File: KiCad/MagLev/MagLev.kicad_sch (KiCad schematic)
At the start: 30 parts, among them J1 Barrel_Jack, Q5 ZX5T1951GTA, U10 DRV5505, U11 DRV5505, U12 DRV5505, U3 L78L05_SO8, U4 TL431A, U5 LM393, X1 L_Ferrite, X2 L_Ferrite, Y1 L_Ferrite, Y2 L_Ferrite

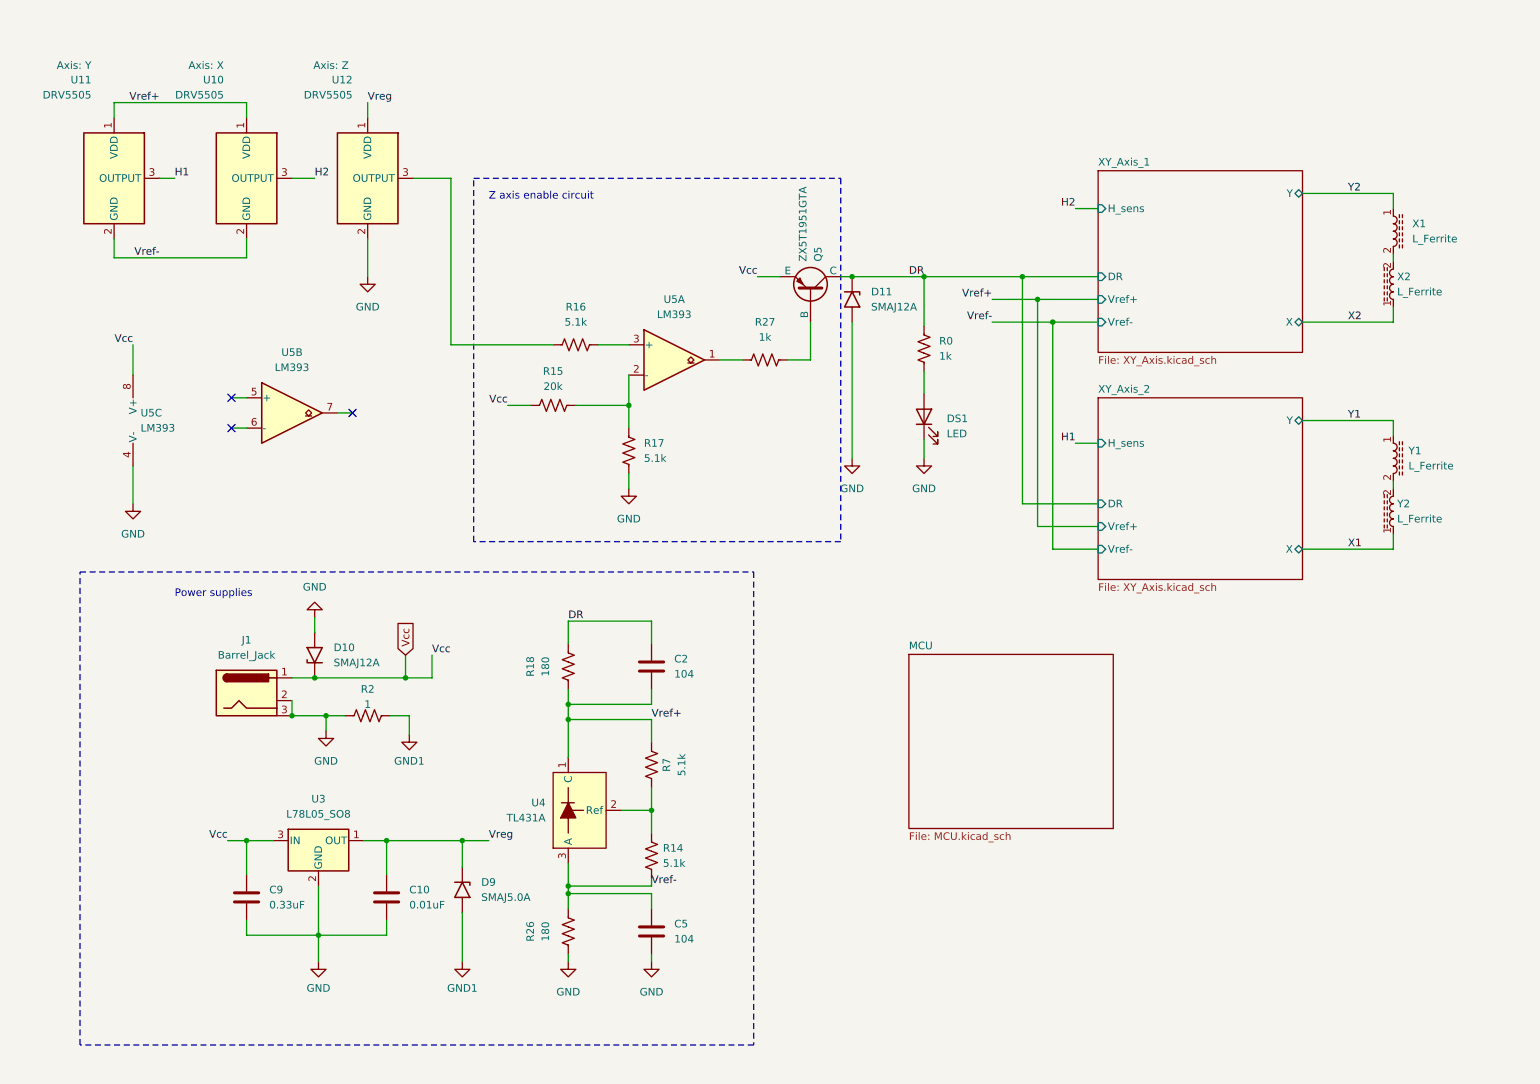
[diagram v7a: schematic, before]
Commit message: Add power fets and additional coils to schematic.
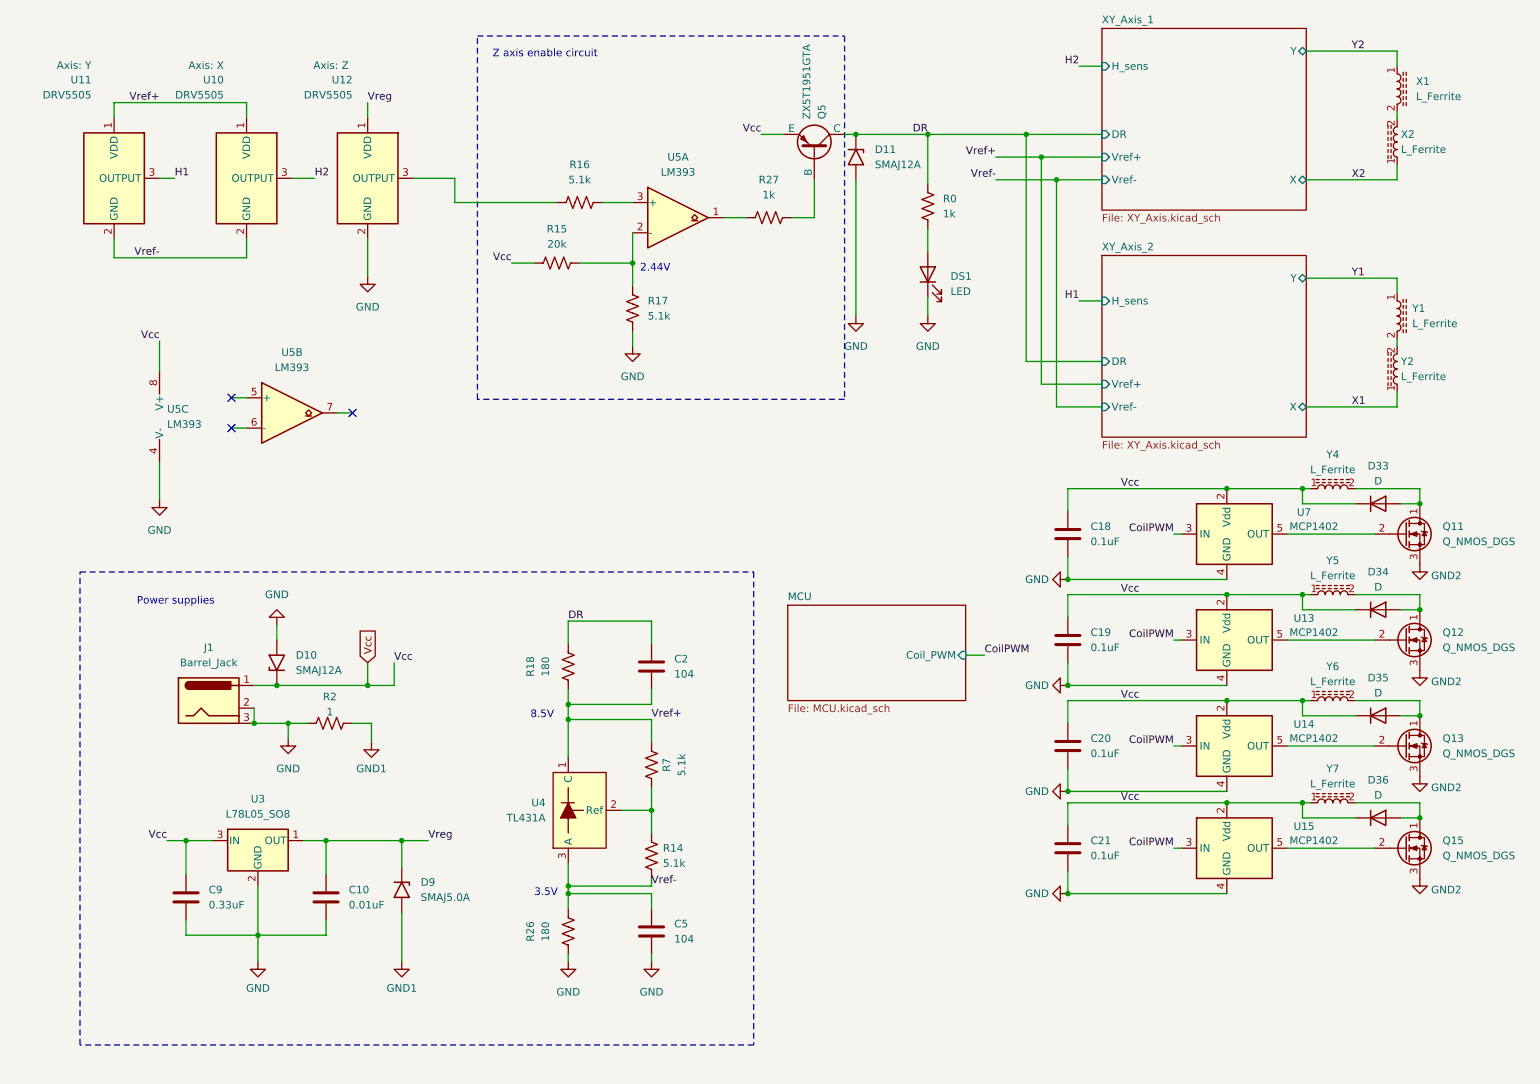
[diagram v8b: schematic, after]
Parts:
- added C18, C19, C20, C21: 0.1uF, Capacitor_SMD:C_0805_2012Metric_Pad1.18x1.45mm_HandSolder, symbol Device:C
- added D33, D34, D35, D36: D, symbol Device:D
- added Q11, Q12, Q13, Q15: Q_NMOS_DGS, symbol Device:Q_NMOS_DGS
- added U13, U14, U15, U7: MCP1402, Package_TO_SOT_SMD:SOT-23-5, symbol Driver_FET:MCP1416
- added Y4, Y5, Y6, Y7: L_Ferrite, Maglev_Footprint_Library:Maglev_coil, symbol Device:L_Ferrite
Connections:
- net GND: now also C18.2, C19.2, C20.2, C21.2, U13.4 (GND), U14.4 (GND), U15.4 (GND), U7.4 (GND)
- net Vcc: now also C18.1, C19.1, C20.1, C21.1, D33.1 (K), D34.1 (K), D35.1 (K), D36.1 (K), U13.2 (Vdd), U14.2 (Vdd), U15.2 (Vdd), U7.2 (Vdd), Y4.1, Y5.1, Y6.1, Y7.1
- new net: D34.2 (A), Q12.1 (D), Y5.2
- new net: Q12.2 (G), U13.5 (OUT)
- new net: D36.2 (A), Q15.1 (D), Y7.2
- new net: Q15.2 (G), U15.5 (OUT)
- new net: Q11.2 (G), U7.5 (OUT)
- new net: D35.2 (A), Q13.1 (D), Y6.2
- new net: Q13.2 (G), U14.5 (OUT)
- new net: D33.2 (A), Q11.1 (D), Y4.2
- new net CoilPWM: U13.3 (IN), U14.3 (IN), U15.3 (IN), U7.3 (IN)
- new net GND2: Q11.3 (S), Q12.3 (S), Q13.3 (S), Q15.3 (S)
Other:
- sheet MCU ports: added Coil_PWM; removed none
- note added: "2.44V"
- note added: "3.5V"
- note added: "8.5V"
- moved on the sheet: C10, C9, D10, D11, D9, DS1, J1, Q5, R0, R15, R16, R17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
